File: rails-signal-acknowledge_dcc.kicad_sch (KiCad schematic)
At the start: 4 parts, among them Q1301 BSS138W

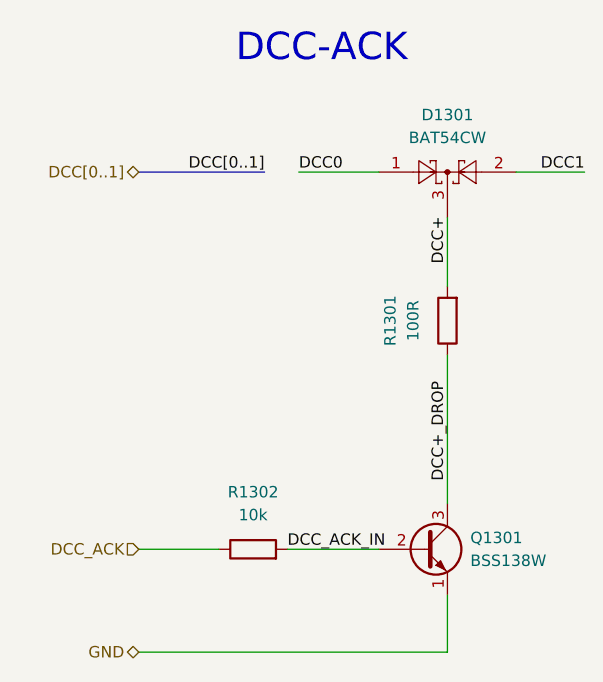
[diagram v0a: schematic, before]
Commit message: Fix - Ignore double power flags
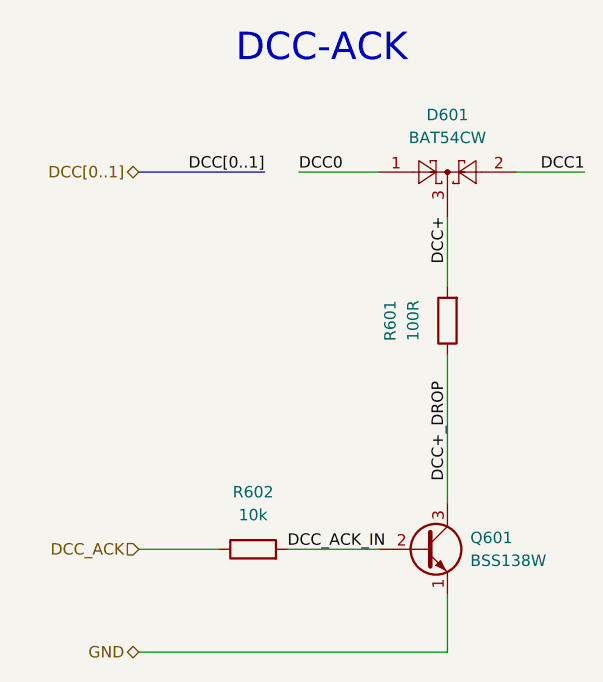
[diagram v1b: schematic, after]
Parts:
- renumbered D1301 to D601, Q1301 to Q601, R1301 to R601, R1302 to R602
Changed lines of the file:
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@@
 		(on_board yes)
 		(dnp no)
-		(property "Reference" "R1301"
+		(property "Reference" "R601"
 			(at 62.23 53.34 90)
 			(effects
@@
 			(project "xDuinoRails-Fortuna-M"
 				(path "/fb33ec4e-6596-45d2-a121-8d3475acd69a/c9229de7-1ed3-435d-9b11-33fa2e05ec65/deaf1b68-8bb1-4a22-bf5f-eab4be33579f"
-					(reference "R1301")
+					(reference "R601")
 					(unit 1)
 				)
@@
 		(dnp no)
 		(fields_autoplaced yes)
-		(property "Reference" "D1301"
+		(property "Reference" "D601"
 			(at 68.58 30.48 0)
 			(effects
@@
 			(project "xDuinoRails-Fortuna-M"
 				(path "/fb33ec4e-6596-45d2-a121-8d3475acd69a/c9229de7-1ed3-435d-9b11-33fa2e05ec65/deaf1b68-8bb1-4a22-bf5f-eab4be33579f"
-					(reference "D1301")
+					(reference "D601")
 					(unit 1)
 				)
@@
 		(on_board yes)
 		(dnp no)
-		(property "Reference" "R1302"
+		(property "Reference" "R602"
 			(at 46.99 72.39 90)
 			(effects
@@
 			(project "xDuinoRails-Fortuna-M"
 				(path "/fb33ec4e-6596-45d2-a121-8d3475acd69a/c9229de7-1ed3-435d-9b11-33fa2e05ec65/deaf1b68-8bb1-4a22-bf5f-eab4be33579f"
-					(reference "R1302")
+					(reference "R602")
 					(unit 1)
 				)
@@
 		(on_board yes)
 		(dnp no)
-		(property "Reference" "Q1301"
+		(property "Reference" "Q601"
 			(at 71.12 77.47 0)
 			(effects
@@
 			(project "xDuinoRails-Fortuna-M"
 				(path "/fb33ec4e-6596-45d2-a121-8d3475acd69a/c9229de7-1ed3-435d-9b11-33fa2e05ec65/deaf1b68-8bb1-4a22-bf5f-eab4be33579f"
-					(reference "Q1301")
+					(reference "Q601")
 					(unit 1)
 				)

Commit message: Fix - Unconnected lines excluded
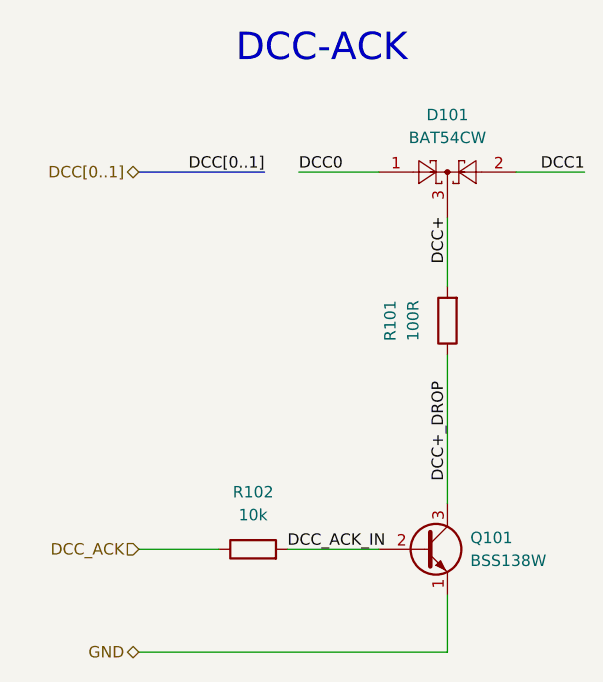
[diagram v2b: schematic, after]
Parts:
- renumbered D601 to D101, Q601 to Q101, R601 to R101, R602 to R102
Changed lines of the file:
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@@
 		(on_board yes)
 		(dnp no)
-		(property "Reference" "R601"
+		(property "Reference" "R101"
 			(at 62.23 53.34 90)
 			(effects
@@
 		)
 		(instances
+			(project "rails-signal-acknowledge_dcc"
+				(path "/e494a89a-0a39-499b-b7b0-4f61cfd00d18"
+					(reference "R101")
+					(unit 1)
+				)
+			)
 			(project "xDuinoRails-Fortuna-M"
 				(path "/fb33ec4e-6596-45d2-a121-8d3475acd69a/c9229de7-1ed3-435d-9b11-33fa2e05ec65/deaf1b68-8bb1-4a22-bf5f-eab4be33579f"
@@
 		(dnp no)
 		(fields_autoplaced yes)
-		(property "Reference" "D601"
+		(property "Reference" "D101"
 			(at 68.58 30.48 0)
 			(effects
@@
 		)
 		(instances
+			(project "rails-signal-acknowledge_dcc"
+				(path "/e494a89a-0a39-499b-b7b0-4f61cfd00d18"
+					(reference "D101")
+					(unit 1)
+				)
+			)
 			(project "xDuinoRails-Fortuna-M"
 				(path "/fb33ec4e-6596-45d2-a121-8d3475acd69a/c9229de7-1ed3-435d-9b11-33fa2e05ec65/deaf1b68-8bb1-4a22-bf5f-eab4be33579f"
@@
 		(on_board yes)
 		(dnp no)
-		(property "Reference" "R602"
+		(property "Reference" "R102"
 			(at 46.99 72.39 90)
 			(effects
@@
 		)
 		(instances
+			(project "rails-signal-acknowledge_dcc"
+				(path "/e494a89a-0a39-499b-b7b0-4f61cfd00d18"
+					(reference "R102")
+					(unit 1)
+				)
+			)
 			(project "xDuinoRails-Fortuna-M"
 				(path "/fb33ec4e-6596-45d2-a121-8d3475acd69a/c9229de7-1ed3-435d-9b11-33fa2e05ec65/deaf1b68-8bb1-4a22-bf5f-eab4be33579f"
@@
 		(on_board yes)
 		(dnp no)
-		(property "Reference" "Q601"
+		(property "Reference" "Q101"
 			(at 71.12 77.47 0)
 			(effects
@@
 		)
 		(instances
+			(project "rails-signal-acknowledge_dcc"
+				(path "/e494a89a-0a39-499b-b7b0-4f61cfd00d18"
+					(reference "Q101")
+					(unit 1)
+				)
+			)
 			(project "xDuinoRails-Fortuna-M"
 				(path "/fb33ec4e-6596-45d2-a121-8d3475acd69a/c9229de7-1ed3-435d-9b11-33fa2e05ec65/deaf1b68-8bb1-4a22-bf5f-eab4be33579f"
@@
 		)
 	)
+	(sheet_instances
+		(path "/"
+			(page "1")
+		)
+	)
